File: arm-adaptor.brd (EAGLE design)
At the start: 3 parts, among them IC2 ATMEGA644-20PU

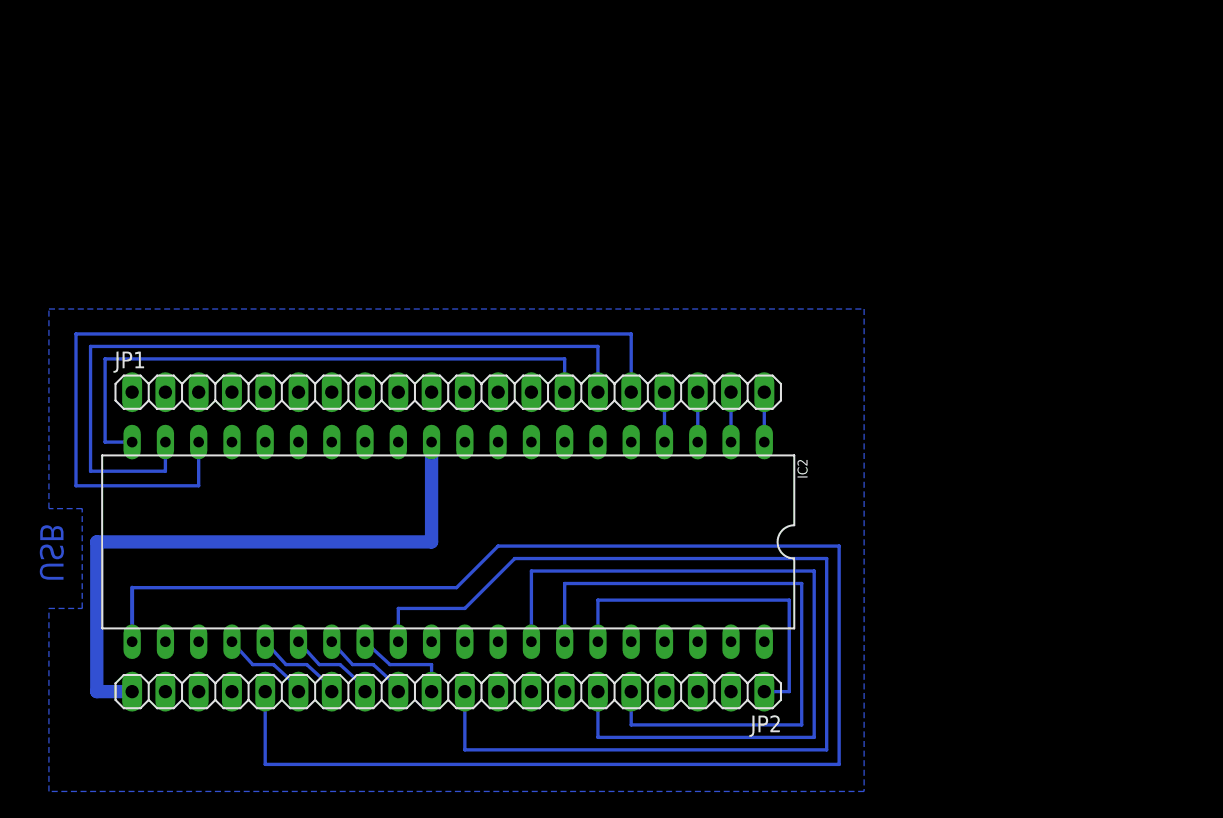
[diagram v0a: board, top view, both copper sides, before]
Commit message: Added SD card and potential dividers on analogue inputs.
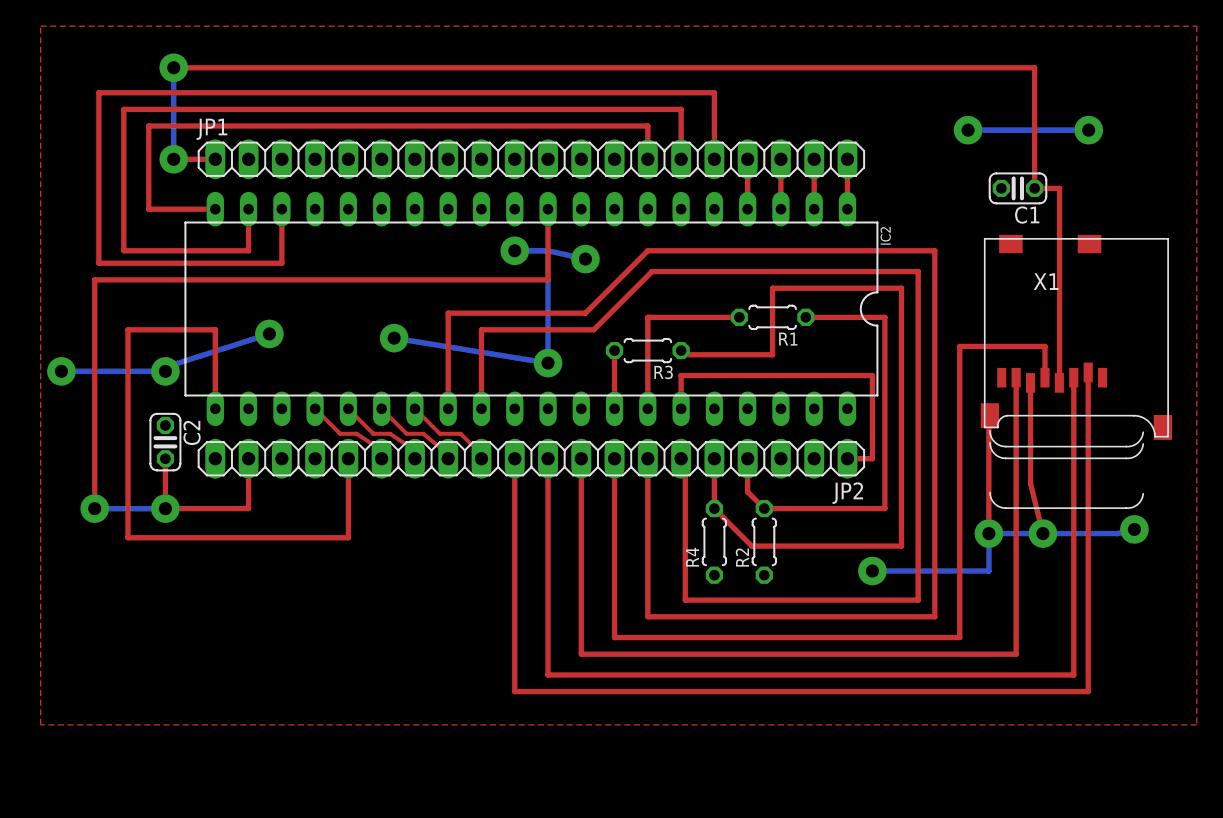
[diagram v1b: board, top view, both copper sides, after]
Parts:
- added C1, C2: 0.1u, rcl:C025-024X044
- added R1, R3: 100K, rcl:0204/5
- added R2, R4: 150K, rcl:0204/5
- added X1: MICROSD, adafruit:MICROSD
- moved IC2 18.9 mm to (33.0, 30.5)
- moved JP2 18.9 mm to (33.0, 19.1)
- moved JP1 18.9 mm to (33.0, 41.9)
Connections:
- removed net VCC: IC2.10
- new net CS: JP2.11, X1.2
- new net MISO: JP2.9, X1.7
- new net MOSI: JP2.10, X1.3
- new net N$1: JP2.4, R1.1, R2.2
- new net N$2: JP2.5, R3.1, R4.2
- new net SCK: JP2.8, X1.5
- new net VDD: C1.1, JP1.1, X1.4
- new net VIN: C2.2, IC2.10, JP2.19
- net B-THERM: now also R1.2; no longer JP2.5
- net E-THERM: now also R3.2; no longer JP2.6
- net GND: now also C1.2, C2.1, R2.1, R4.1, X1.6, X1.MT1, X1.MT2
- net Y-DIR: now also JP2.6; no longer JP2.10
- net Y-STEP: now also JP2.7; no longer JP2.11
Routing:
- net VDD: track 0.00 -> 101.9 mm, vias 0 -> 2
- net Y-STEP: track 7.82 -> 108.3 mm
- net CS: track 0.00 -> 85.9 mm
- net MOSI: track 0.00 -> 79.3 mm
- net VIN: track 0.00 -> 76.8 mm, vias 0 -> 2
- net X-STEP: track 125.5 -> 51.4 mm
- net SCK: track 0.00 -> 71.1 mm
- net MISO: track 0.00 -> 69.2 mm
- net N$2: track 0.00 -> 61.2 mm
- net E-THERM: track 59.7 -> 4.45 mm
- net GND: track 47.3 -> 95.9 mm, vias 0 -> 13
- net B-THERM: track 48.9 -> 14.0 mm
- net N$1: track 0.00 -> 34.2 mm
- net !HOTBED: track 71.1 -> 83.2 mm
- net Y-DIR: track 83.5 -> 95.2 mm
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- added copper zone on layer 1, net GND
- removed copper zone on layer 16, net GND
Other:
- board text removed: "USB"
